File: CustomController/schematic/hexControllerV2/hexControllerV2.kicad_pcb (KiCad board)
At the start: 2 copper layers, 129 x 63.9 mm, 48 parts, among them IC1 ESP32-S2-MINI-1-N4R2, IC2 IP5306, J1 USB_C_Receptacle_USB2.0_16P, J2 Battery, J3 Switch1, J4 Switch2, J5 Switch3, J6 Switch4, J7 Battery, SW1 RotaryEncoder_Switch, SW2 SW_DIP_x01, SW3 SW_DIP_x01, SW4 SW_DIP_x01, SW5 SW_DIP_x01, SW6 SW_DIP_x01, U2 AMS1117-3.3

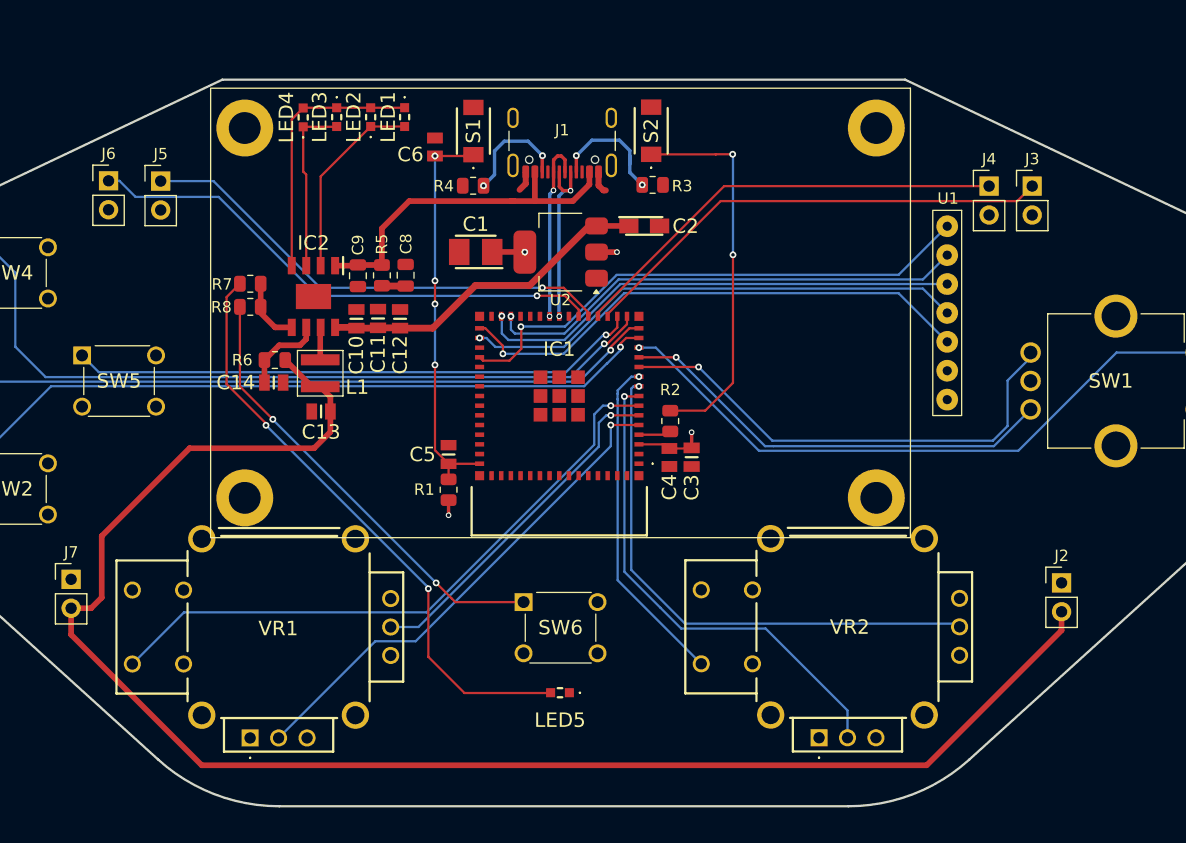
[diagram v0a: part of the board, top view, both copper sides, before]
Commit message: Reworking schematic
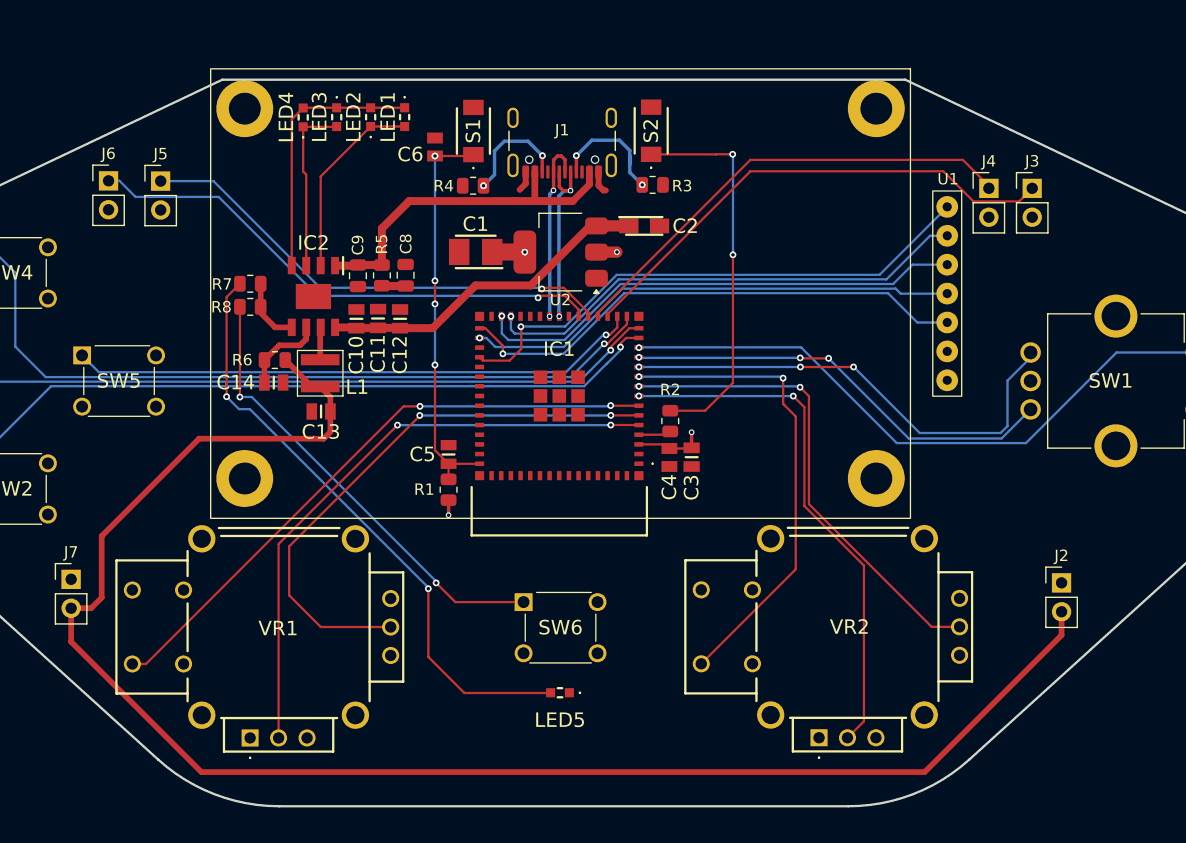
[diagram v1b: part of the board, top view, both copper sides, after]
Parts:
- moved U1 1.70 mm to (156.4, 69.8)
- moved J4 0.20 mm to (190.0, 60.5)
- moved J3 0.20 mm to (193.8, 60.5)
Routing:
- net Joy1Y: track 30.7 -> 49.9 mm, vias 1 -> 2
- net Joy2Button: track 29.4 -> 41.7 mm, vias 1 -> 2
- net Joy1X: track 44.1 -> 53.0 mm, vias 1 -> 2
- net Joy2Y: track 47.6 -> 42.5 mm, vias 1 -> 2
- net Joy2X: track 43.8 -> 46.8 mm, vias 1 -> 2
- net +5V USB: track 34.4 -> 32.0 mm
- net Switch1: track 42.2 -> 44.3 mm
- net Switch2: track 39.3 -> 41.2 mm
- net Joy1Button: track 55.5 -> 53.9 mm, vias 1 -> 2
- net Net-(J2-Pin_2): track 141.5 -> 142.6 mm
- net CS: track 43.0 -> 43.9 mm
- net DC: track 42.5 -> 43.4 mm
- net Net-(R8-Pad2): track 39.8 -> 40.4 mm
- net EncoderB: track 39.0 -> 38.4 mm, vias 1 -> 3
- net EncoderA: track 42.9 -> 42.3 mm, vias 1 -> 3
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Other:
- copper layers 2 -> 4
